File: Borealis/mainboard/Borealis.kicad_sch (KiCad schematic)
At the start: 7 parts, among them J1 Conn_01x06_Pin, J3 Conn_01x02_Pin, J4 Conn_01x08_Pin, U1 Pico

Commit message: fixed some stuff
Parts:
- J1: value Conn_01x06_Pin -> Conn_01x06_Pin (sensor board connection); footprint (none) -> Connector_JST:JST_PH_B6B-PH-K_1x06_P2.00mm_Vertical
- J3: value Conn_01x02_Pin -> Conn_01x02_Pin (power input); footprint (none) -> Connector_JST:JST_JWPF_B02B-JWPF-SK-R_1x02_P2.00mm_Vertical
- J4: value Conn_01x08_Pin -> Conn_01x08_Pin (control panel connection); footprint (none) -> Connector_PinHeader_2.54mm:PinHeader_1x08_P2.54mm_Vertical
- R1, R2, R3: footprint (none) -> OptoDevice:R_LDR_4.9x4.2mm_P2.54mm_Vertical
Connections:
- net at U1.3 (GND): no longer J4.1 (Pin_1)
- net +3.3V: now reaches J1.2 (Pin_2), J4.2 (Pin_2), U1.37 (3V3_EN)
- net GND: now reaches J1.1 (Pin_1), R3.2, U1.38 (GND)
- net GND: now also J4.1 (Pin_1)
- net +5V: now reaches J1.3 (Pin_3), J3.2 (Pin_2), U1.40 (VBUS)
- net ADC: now reaches J1.6 (Pin_6), R3.1, U1.32 (GPIO27_ADC1)

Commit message: Added sensor board
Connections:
- net SDA: now also J1.5 (Pin_5), J4.4 (Pin_4), U1.1 (GPIO0)
- net SCL: now reaches J1.4 (Pin_4), J4.3 (Pin_3), U1.2 (GPIO1)
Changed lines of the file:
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@@
 	(generator_version "9.0")
 	(paper "A4")
-	(junction
-		(at 71.12 90.17)
-		(diameter 0)
-		(color 0 0 0 0)
-	)
-	(junction
-		(at 68.58 92.71)
-		(diameter 0)
-		(color 0 0 0 0)
-	)
 	(wire
 		(pts
@@
 	(wire
 		(pts
-			(xy 100.33 74.93) (xy 68.58 74.93)
-		)
-		(stroke
-			(width 0)
-			(type default)
-		)
-	)
-	(wire
-		(pts
 			(xy 41.91 154.94) (xy 41.91 81.28)
 		)
@@
 	(wire
 		(pts
-			(xy 74.93 92.71) (xy 68.58 92.71)
-		)
-		(stroke
-			(width 0)
-			(type default)
-		)
-	)
-	(wire
-		(pts
 			(xy 110.49 149.86) (xy 49.53 149.86)
 		)
@@
 	(wire
 		(pts
-			(xy 91.44 55.88) (xy 91.44 72.39)
-		)
-		(stroke
-			(width 0)
-			(type default)
-		)
-	)
-	(wire
-		(pts
-			(xy 71.12 90.17) (xy 58.42 90.17)
-		)
-		(stroke
-			(width 0)
-			(type default)
-		)
-	)
-	(wire
-		(pts
 			(xy 41.91 73.66) (xy 41.91 52.07)
 		)
@@
 	(wire
 		(pts
-			(xy 60.96 59.69) (xy 73.66 59.69)
+			(xy 67.31 90.17) (xy 74.93 90.17)
+		)
+		(stroke
+			(width 0)
+			(type default)
+		)
+	)
+	(wire
+		(pts
+			(xy 68.58 59.69) (xy 73.66 59.69)
 		)
 		(stroke
@@
 	(wire
 		(pts
+			(xy 68.58 57.15) (xy 73.66 57.15)
+		)
+		(stroke
+			(width 0)
+			(type default)
+		)
+	)
+	(wire
+		(pts
 			(xy 69.85 64.77) (xy 73.66 64.77)
 		)
@@
 	(wire
 		(pts
-			(xy 58.42 57.15) (xy 73.66 57.15)
-		)
-		(stroke
-			(width 0)
-			(type default)
-		)
-	)
-	(wire
-		(pts
-			(xy 68.58 74.93) (xy 68.58 92.71)
-		)
-		(stroke
-			(width 0)
-			(type default)
-		)
-	)
-	(wire
-		(pts
-			(xy 58.42 90.17) (xy 58.42 57.15)
-		)
-		(stroke
-			(width 0)
-			(type default)
-		)
-	)
-	(wire
-		(pts
-			(xy 100.33 58.42) (xy 100.33 74.93)
-		)
-		(stroke
-			(width 0)
-			(type default)
-		)
-	)
-	(wire
-		(pts
-			(xy 91.44 72.39) (xy 71.12 72.39)
-		)
-		(stroke
-			(width 0)
-			(type default)
-		)
-	)
-	(wire
-		(pts
 			(xy 114.3 154.94) (xy 41.91 154.94)
 		)
@@
 	(wire
 		(pts
-			(xy 137.16 55.88) (xy 91.44 55.88)
-		)
-		(stroke
-			(width 0)
-			(type default)
-		)
-	)
-	(wire
-		(pts
 			(xy 55.88 49.53) (xy 73.66 49.53)
 		)
@@
 	(wire
 		(pts
+			(xy 130.81 58.42) (xy 137.16 58.42)
+		)
+		(stroke
+			(width 0)
+			(type default)
+		)
+	)
+	(wire
+		(pts
 			(xy 110.49 90.17) (xy 113.03 90.17)
 		)
@@
 	(wire
 		(pts
-			(xy 68.58 92.71) (xy 60.96 92.71)
+			(xy 67.31 92.71) (xy 74.93 92.71)
 		)
 		(stroke
@@
 	(wire
 		(pts
-			(xy 60.96 92.71) (xy 60.96 59.69)
-		)
-		(stroke
-			(width 0)
-			(type default)
-		)
-	)
-	(wire
-		(pts
 			(xy 110.49 135.89) (xy 114.3 135.89)
 		)
@@
 	(wire
 		(pts
-			(xy 71.12 72.39) (xy 71.12 90.17)
-		)
-		(stroke
-			(width 0)
-			(type default)
-		)
-	)
-	(wire
-		(pts
-			(xy 137.16 58.42) (xy 100.33 58.42)
-		)
-		(stroke
-			(width 0)
-			(type default)
-		)
-	)
-	(wire
-		(pts
 			(xy 68.58 62.23) (xy 73.66 62.23)
 		)
@@
 	(wire
 		(pts
-			(xy 74.93 90.17) (xy 71.12 90.17)
-		)
-		(stroke
-			(width 0)
-			(type default)
-		)
-	)
-	(wire
-		(pts
 			(xy 119.38 160.02) (xy 36.83 160.02)
+		)
+		(stroke
+			(width 0)
+			(type default)
+		)
+	)
+	(wire
+		(pts
+			(xy 130.81 55.88) (xy 137.16 55.88)
 		)
 		(stroke
@@
 		)
 	)
+	(label "SCL"
+		(at 67.31 92.71 0)
+		(effects
+			(font
+				(size 1.27 1.27)
+			)
+			(justify left bottom)
+		)
+	)
 	(label "ADC"
 		(at 114.3 110.49 0)
@@
 		)
 	)
+	(label "SCL"
+		(at 68.58 59.69 0)
+		(effects
+			(font
+				(size 1.27 1.27)
+			)
+			(justify left bottom)
+		)
+	)
 	(label "SDA"
-		(at 62.23 101.6 0)
+		(at 68.58 57.15 0)
+		(effects
+			(font
+				(size 1.27 1.27)
+			)
+			(justify left bottom)
+		)
+	)
+	(label "SDA"
+		(at 67.31 90.17 0)
+		(effects
+			(font
+				(size 1.27 1.27)
+			)
+			(justify left bottom)
+		)
+	)
+	(label "SCL"
+		(at 130.81 58.42 0)
 		(effects
 			(font
@@
 		(effects
 			(font
+				(size 1.27 1.27)
+			)
+			(justify left bottom)
+		)
+	)
+	(label "SDA"
+		(at 130.81 55.88 0)
+		(effects
+			(font

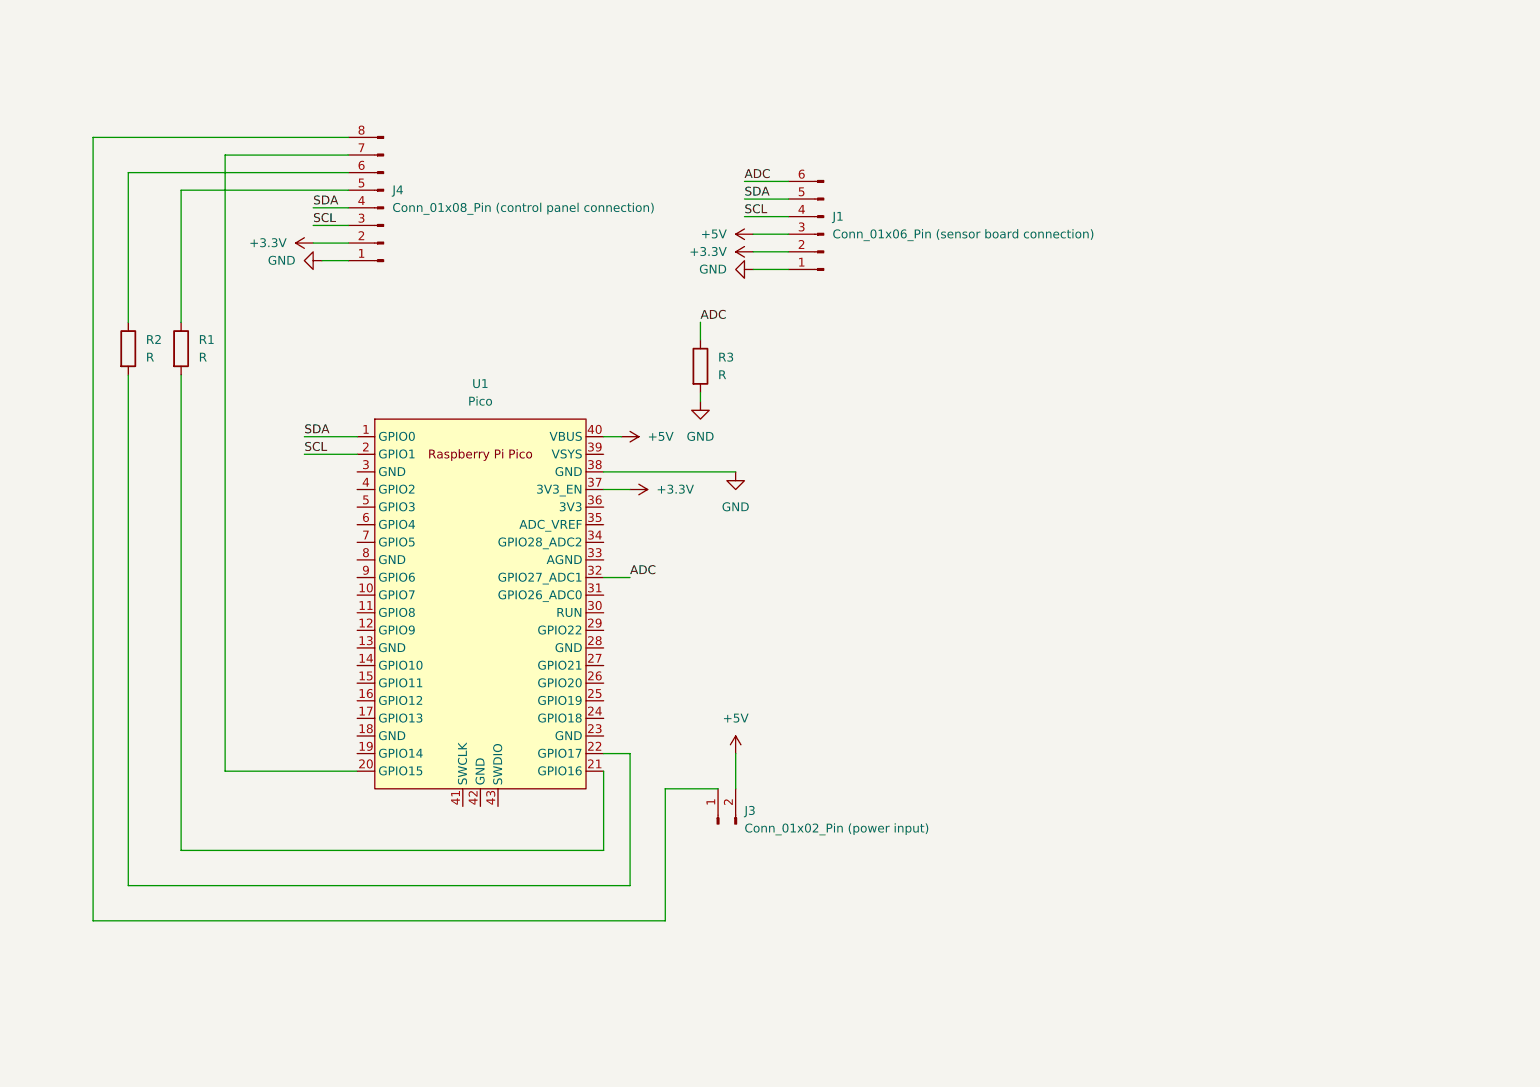
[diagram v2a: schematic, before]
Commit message: Changed main board based on what was discussed during the hardware meeting
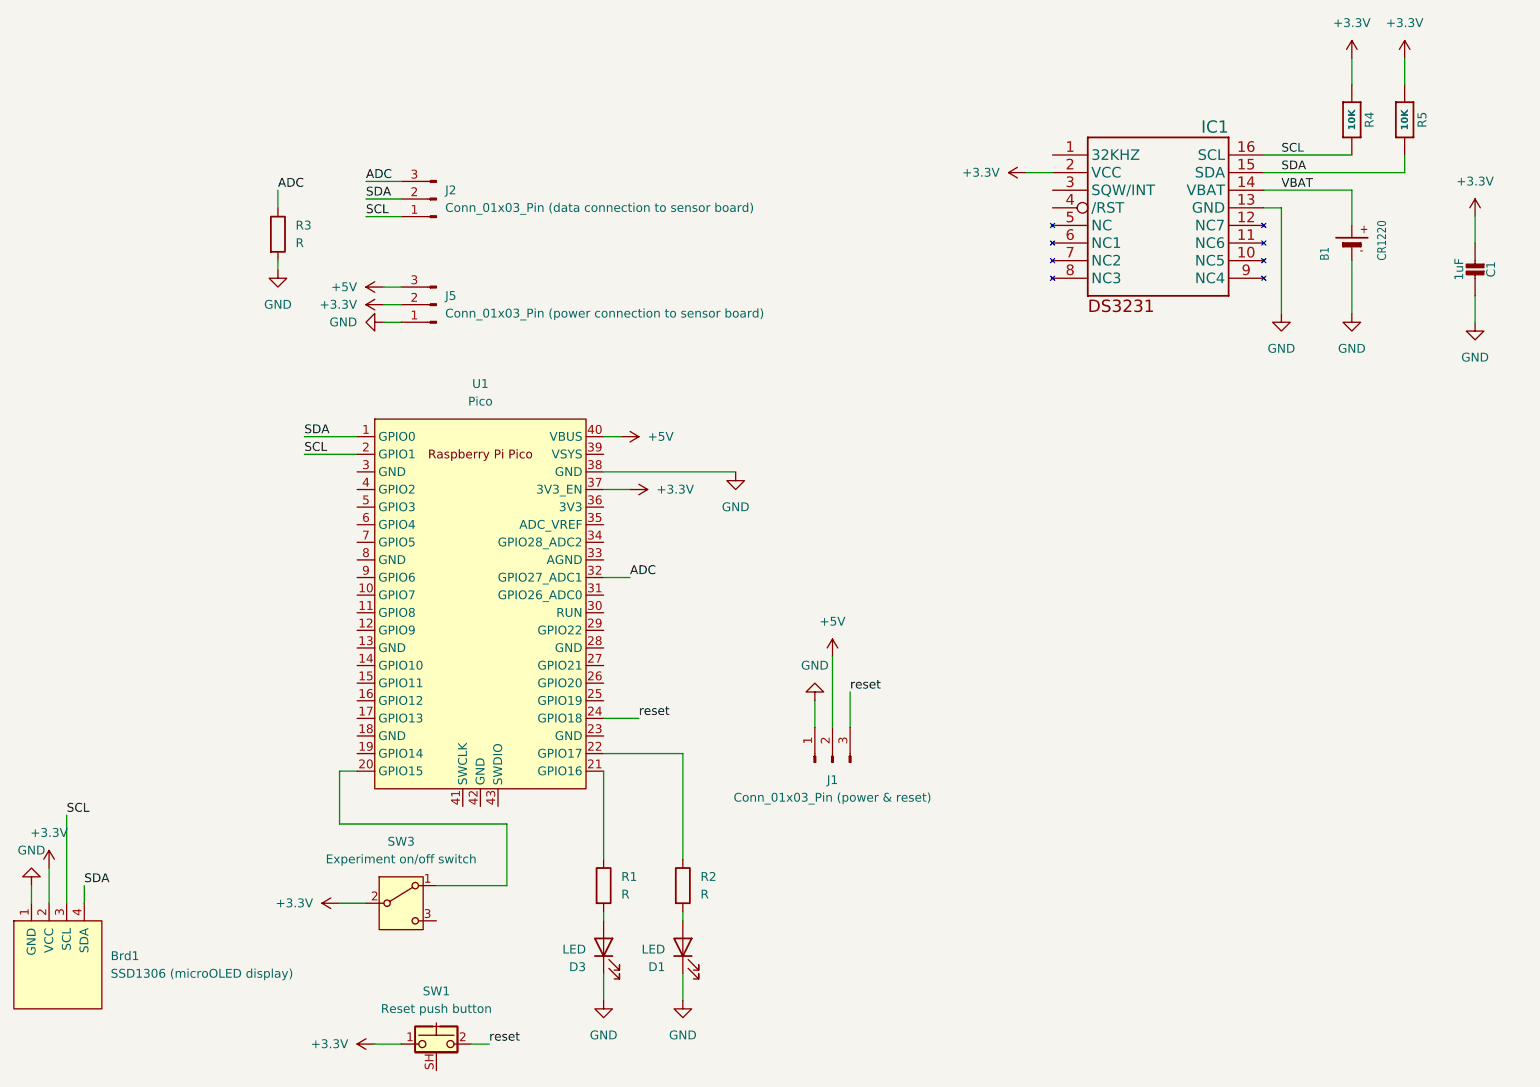
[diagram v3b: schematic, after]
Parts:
- removed J1: Conn_01x06_Pin (sensor board connection), Connector_JST:JST_PH_B6B-PH-K_1x06_P2.00mm_Vertical, symbol Connector:Conn_01x06_Pin
- removed J3: Conn_01x02_Pin (power input), Connector_JST:JST_JWPF_B02B-JWPF-SK-R_1x02_P2.00mm_Vertical, symbol Connector:Conn_01x02_Pin
- removed J4: Conn_01x08_Pin (control panel connection), Connector_PinHeader_2.54mm:PinHeader_1x08_P2.54mm_Vertical, symbol Connector:Conn_01x08_Pin
- added B1: CR1220, Adafruit DS3231 RTC Breakout:CR1220, symbol Adafruit DS3231 RTC Breakout-eagle-import:BATTERYCR1220_SMT
- added Brd1: SSD1306 (microOLED display), TG9541:Display_128x64_096_I2C, symbol SSD1306-128x64_OLED:SSD1306
- added C1: 1uF, Adafruit DS3231 RTC Breakout:0805-NO, symbol Adafruit DS3231 RTC Breakout-eagle-import:CAP_CERAMIC0805-NOOUTLINE
- added D1, D3: LED, LED_THT:LED_D5.0mm, symbol Device:LED
- added IC1: DS3231/SO, Adafruit DS3231 RTC Breakout:SO16W, symbol Adafruit DS3231 RTC Breakout-eagle-import:DS3231/SO
- added J1: Conn_01x03_Pin (power & reset), symbol Connector:Conn_01x03_Pin
- added J2: Conn_01x03_Pin (data connection to sensor board), symbol Connector:Conn_01x03_Pin
- added J5: Conn_01x03_Pin (power connection to sensor board), symbol Connector:Conn_01x03_Pin
- added R4, R5: 10K, Adafruit DS3231 RTC Breakout:0805-NO, symbol Adafruit DS3231 RTC Breakout-eagle-import:RESISTOR0805_NOOUTLINE
- added SW1: Reset push button, symbol Switch:SW_Push_Shielded
- added SW3: Experiment on/off switch, Connector_PinHeader_2.54mm:PinHeader_1x03_P2.54mm_Vertical, symbol Switch:SW_SPDT
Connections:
- net +3.3V: now also Brd1.2 (VCC), C1.2, IC1.2 (VCC), J5.2 (Pin_2), R4.1, R5.1, SW1.1, SW3.2 (B)
- net +5V: now also J1.2 (Pin_2), J5.3 (Pin_3)
- net ADC: now also J2.3 (Pin_3)
- net GND: now also B1.-, Brd1.1 (GND), C1.1, D1.1 (K), D3.1 (K), IC1.13 (GND), J1.1 (Pin_1), J5.1 (Pin_1)
- net SCL: now also Brd1.3 (SCL), IC1.16 (SCL), J2.1 (Pin_1), R4.2
- net SDA: now also Brd1.4 (SDA), IC1.15 (SDA), J2.2 (Pin_2), R5.2
- net at R1.1: now also U1.21 (GPIO16)
- net at R2.1: now also U1.22 (GPIO17)
- net at U1.20 (GPIO15): now also SW3.1 (A)
- net at R1.2: now also D3.2 (A); no longer U1.21 (GPIO16)
- net at R2.2: now also D1.2 (A); no longer U1.22 (GPIO17)
- net reset: now reaches U1.24 (GPIO18)
- net reset: now also J1.3 (Pin_3), SW1.2
- new net VBAT: B1.+$1 (+), IC1.14 (VBAT)
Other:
- moved on the sheet: R1, R2, R3

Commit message: Updating changes
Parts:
- removed IC1: DS3231/SO, Adafruit DS3231 RTC Breakout:SO16W, symbol Adafruit DS3231 RTC Breakout-eagle-import:DS3231/SO
- added J3: Conn_01x06_Pin (microSD reader) (to be removed), symbol Connector:Conn_01x06_Pin
- added J4: Conn_02x04_Counter_Clockwise (microSD reader conn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, symbol Connector_Generic:Conn_02x04_Counter_Clockwise
- added U2: DS3231SN#T&R, Package_SO:SOIC-16W_7.5x10.3mm_P1.27mm, symbol DS3231SN#1_DS3231SN#-altium-import:root_0_DS3231SN#T&R_
- B1: footprint Adafruit DS3231 RTC Breakout:CR1220 -> batteryholder:BAT-SMD_CR1220-2
- J1, J2: footprint (none) -> batteryholder:1x03 2.3 pitch
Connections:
- net +3.3V: now also J3.5 (Pin_5), U2.2 (VCC)
- net GND: now also J3.6 (Pin_6), U2.13 (GND)
- net SCL: now also U2.16 (SCL)
- net SDA: now also U2.15 (SDA)
- net VBAT: now also U2.14 (VBAT)
- new net CS: J3.1 (Pin_1)
- new net MISO: J3.4 (Pin_4)
- new net MOSI: J3.3 (Pin_3)
- new net SCK: J3.2 (Pin_2)

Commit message: Added barometric sensor board
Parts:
- R1, R2, R3: footprint OptoDevice:R_LDR_4.9x4.2mm_P2.54mm_Vertical -> Resistor_SMD:R_0805_2012Metric
- R4, R5: footprint Adafruit DS3231 RTC Breakout:0805-NO -> Resistor_SMD:R_0805_2012Metric
- U1: footprint RPi_Pico:RPi_Pico_SMD_TH -> Module:RaspberryPi_Pico_Common_THT
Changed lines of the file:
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@@
 			)
 		)
-		(property "Footprint" "Adafruit DS3231 RTC Breakout:0805-NO"
+		(property "Footprint" "Resistor_SMD:R_0805_2012Metric"
 			(at 226.06 44.45 0)
 			(effects
@@
 			)
 		)
-		(property "Footprint" "Adafruit DS3231 RTC Breakout:0805-NO"
+		(property "Footprint" "Resistor_SMD:R_0805_2012Metric"
 			(at 218.44 44.45 0)
 			(effects
@@
 			)
 		)
-		(property "Footprint" "OptoDevice:R_LDR_4.9x4.2mm_P2.54mm_Vertical"
+		(property "Footprint" "Resistor_SMD:R_0805_2012Metric"
 			(at 108.712 154.94 90)
 			(effects
@@
 			)
 		)
-		(property "Footprint" "OptoDevice:R_LDR_4.9x4.2mm_P2.54mm_Vertical"
+		(property "Footprint" "Resistor_SMD:R_0805_2012Metric"
 			(at 61.722 60.96 90)
 			(effects
@@
 			)
 		)
-		(property "Footprint" "OptoDevice:R_LDR_4.9x4.2mm_P2.54mm_Vertical"
+		(property "Footprint" "Resistor_SMD:R_0805_2012Metric"
 			(at 120.142 154.94 90)
 			(effects
@@
 			)
 		)
-		(property "Footprint" "RPi_Pico:RPi_Pico_SMD_TH"
+		(property "Footprint" "Module:RaspberryPi_Pico_Common_THT"
 			(at 92.71 114.3 90)
 			(effects
